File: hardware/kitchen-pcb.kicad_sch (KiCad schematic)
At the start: 40 parts, among them J1 GSD090012SEU, J2 Conn_02x02_Odd_Even, J3 Conn_01x06, J4 Conn_01x03, Q1 TEMT6000X01, U1 SHT30-DIS-B, U2 MX25L3233FM2I-08G

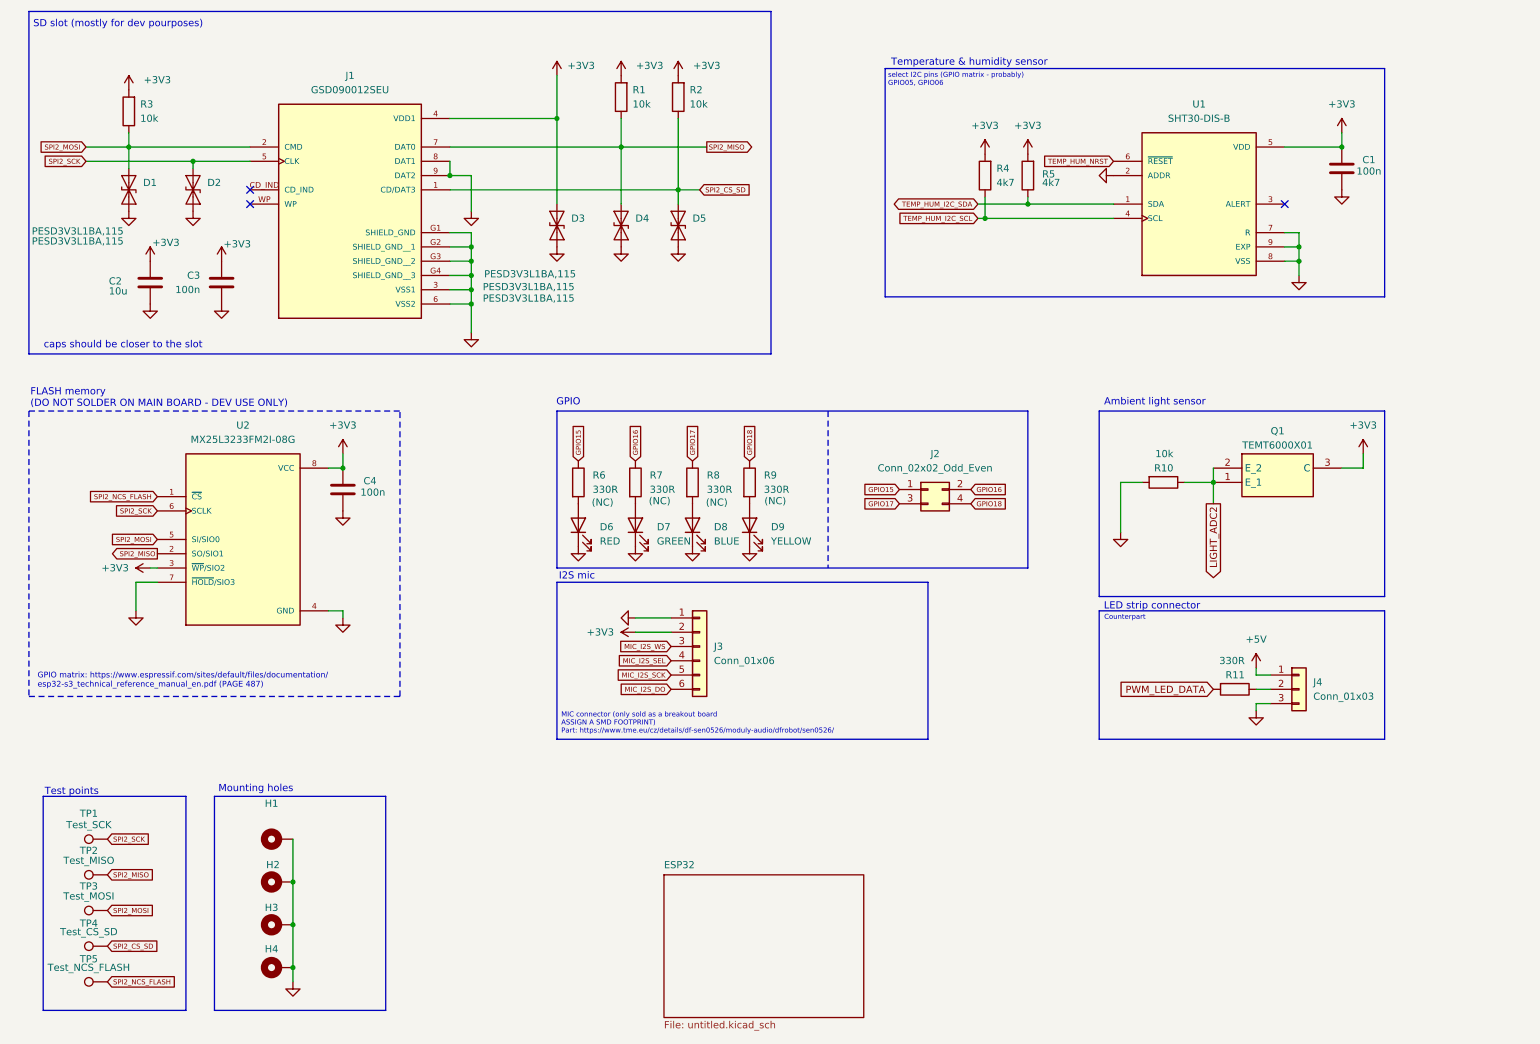
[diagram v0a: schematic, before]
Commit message: Added notes to schematics, SPI modifications
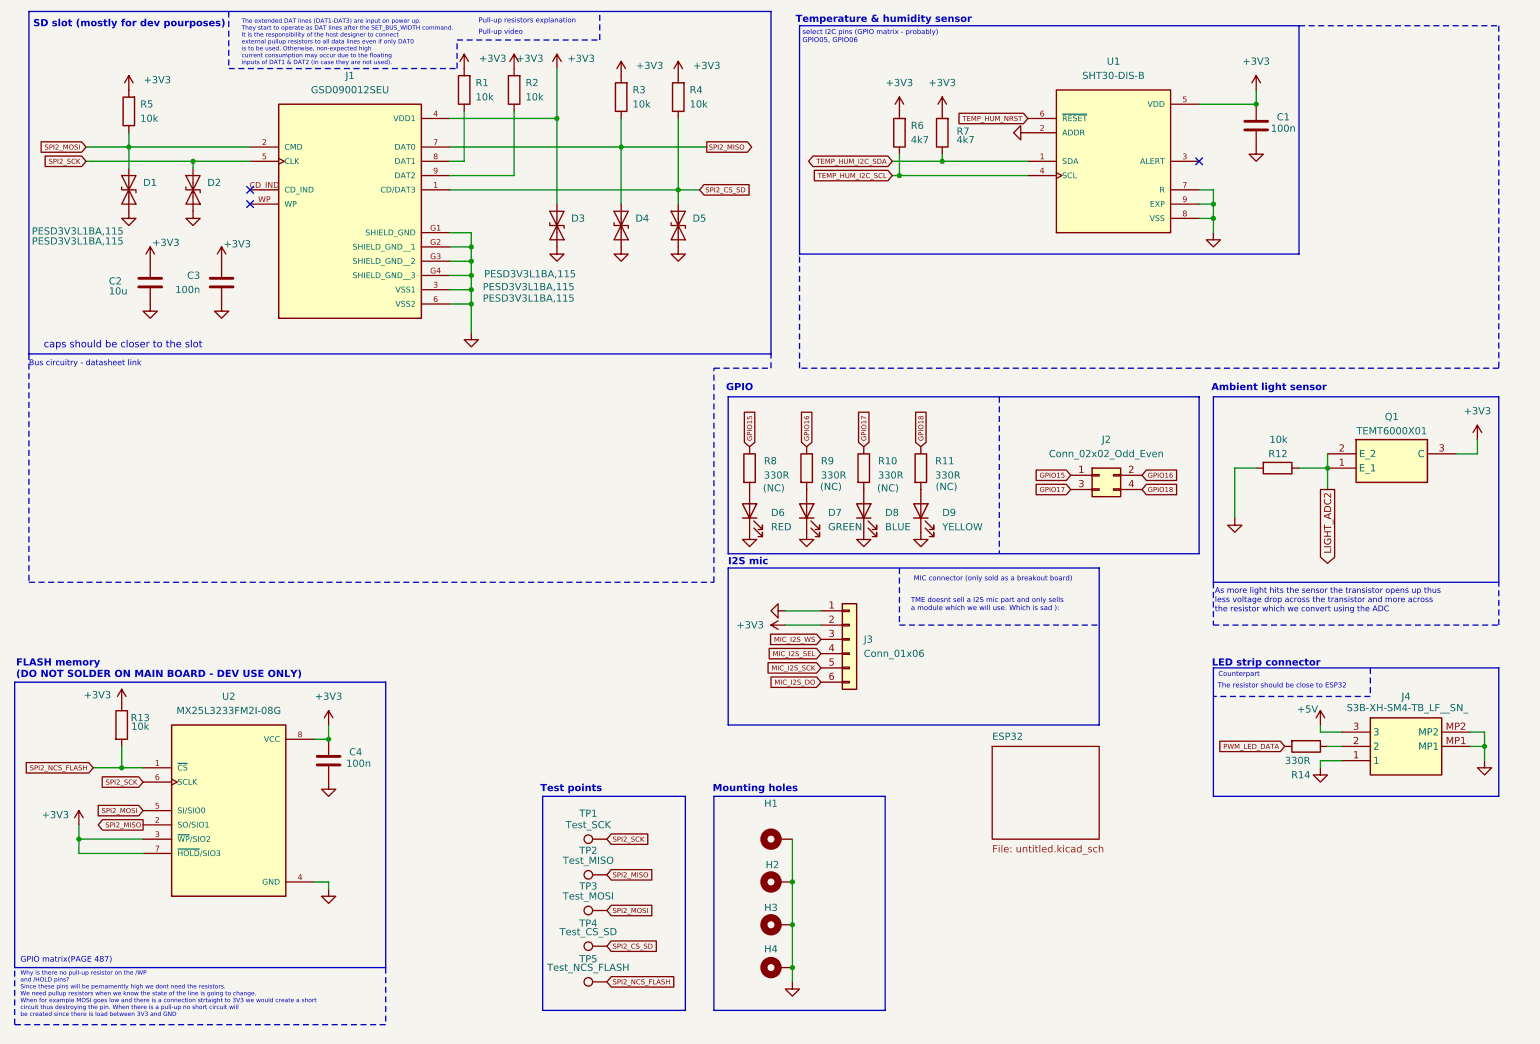
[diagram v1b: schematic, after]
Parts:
- removed J4: Conn_01x03, Connector_JST:JST_XH_S3B-XH-SM4-TB_1x03-1MP_P2.50mm_Horizontal, symbol Connector_Generic:Conn_01x03
- added J4: S3B-XH-SM4-TB_LF__SN_, ESP32-project-footprints:S3BXHSM4TBLFSN, symbol S3B-XH-SM4-TB_LF__SN_:S3B-XH-SM4-TB_LF__SN_
- added R1, R13, R2: 10k, Resistor_SMD:R_0805_2012Metric_Pad1.20x1.40mm_HandSolder, symbol Device:R
- renumbered R8 to R10, R9 to R11, R10 to R12, R11 to R14, R1 to R3, R2 to R4, R3 to R5, R4 to R6, R5 to R7, R6 to R8, R7 to R9
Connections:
- net +3V3: now also U2.7 (~{HOLD}/SIO3), R1.2, R13.1, R2.2
- net +5V: now also J4.3
- net GND: now also J4.1, J4.MP1, J4.MP2; no longer J1.8 (DAT1), J1.9 (DAT2), U2.7 (~{HOLD}/SIO3)
- net SPI2_NCS_FLASH: now also R13.2
- net at R14.1: now also J4.2
- new net: J1.9 (DAT2), R2.1
- new net: J1.8 (DAT1), R1.1
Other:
- note added: "As more light hits the sensor the transistor opens up thus less voltage drop across the transistor and more across the resistor which we convert using the ADC"
- note added: "Bus circuitry - datasheet link"
- note added: "GPIO matrix(PAGE 487)"
- note added: "MIC connector (only sold as a breakout board)"
- note added: "Pull-up resistors explanation"
- note added: "Pull-up video"
- note added: "TME doesnt sell a I2S mic part and only sells a module which we will use. Which is sad ):"
- note added: "The extended DAT lines (DAT1-DAT3) are input on power up. They start to operate as DAT lines after the SET_BUS_WIDTH command. It is the responsibility of the host designer to connect external pullup resistors to all data lines even if only DAT0 is to be used. Otherwise, non-expected high current consumption may occur due to the floating inputs of DAT1 & DAT2 (in case they are not used)."
- note added: "The resistor should be close to ESP32"
- note added: "Why is there no pull-up resistor on the /WP and /HOLD pins? Since these pins will be pernamently high we dont need the resistors. We need pullup resistors when we know the state of the line is going to change. When for example MOSI goes low and there is a connection strtaight to 3V3 we would create a short circuit thus destroying the pin. When there is a pull-up no short circuit will be created s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"
- note removed: "GPIO matrix: https://www.espressif.com/sites/default/files/documentation/ esp32-s3_technical_reference_manual_en.pdf (PAGE 487)"
- note removed: "MIC connector (only sold as a breakout board ASSIGN A SMD FOOTPRINT) Part: https://www.tme.eu/cz/details/df-sen0526/moduly-audio/dfrobot/sen0526/"
- moved on the sheet: C1, C4, D6, D7, D8, D9, H1, H2, H3, H4, J2, J3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

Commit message: Layout v0,4
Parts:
- TP1, TP2, TP3, TP4, TP5: footprint TestPoint:TestPoint_THTPad_D3.0mm_Drill1.5mm -> TestPoint:TestPoint_THTPad_D2.0mm_Drill1.0mm
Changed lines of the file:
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@@
 			)
 		)
-		(property "Footprint" "TestPoint:TestPoint_THTPad_D3.0mm_Drill1.5mm"
+		(property "Footprint" "TestPoint:TestPoint_THTPad_D2.0mm_Drill1.0mm"
 			(at 123.19 182.88 0)
 			(effects
@@
 			)
 		)
-		(property "Footprint" "TestPoint:TestPoint_THTPad_D3.0mm_Drill1.5mm"
+		(property "Footprint" "TestPoint:TestPoint_THTPad_D2.0mm_Drill1.0mm"
 			(at 123.19 157.48 0)
 			(effects
@@
 			)
 		)
-		(property "Footprint" "TestPoint:TestPoint_THTPad_D3.0mm_Drill1.5mm"
+		(property "Footprint" "TestPoint:TestPoint_THTPad_D2.0mm_Drill1.0mm"
 			(at 123.19 176.53 0)
 			(effects
@@
 			)
 		)
-		(property "Footprint" "TestPoint:TestPoint_THTPad_D3.0mm_Drill1.5mm"
+		(property "Footprint" "TestPoint:TestPoint_THTPad_D2.0mm_Drill1.0mm"
 			(at 123.19 170.18 0)
 			(effects
@@
 			)
 		)
-		(property "Footprint" "TestPoint:TestPoint_THTPad_D3.0mm_Drill1.5mm"
+		(property "Footprint" "TestPoint:TestPoint_THTPad_D2.0mm_Drill1.0mm"
 			(at 123.19 163.83 0)
 			(effects

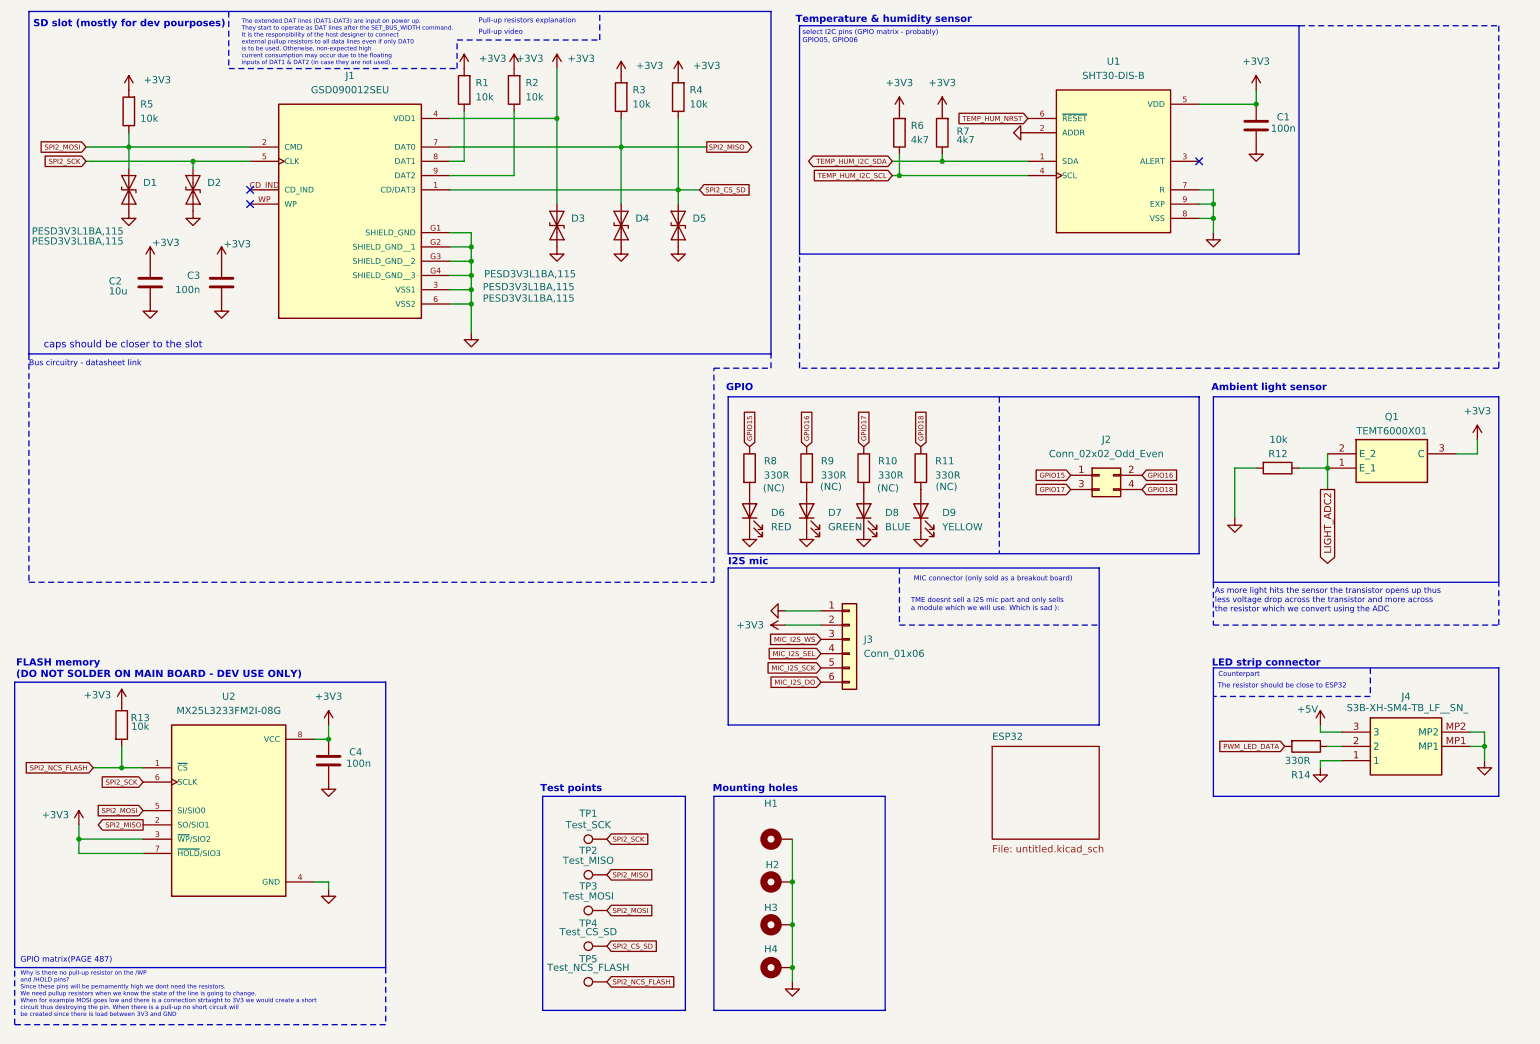
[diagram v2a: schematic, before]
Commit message: Changed to microSD, layout v0.6.1
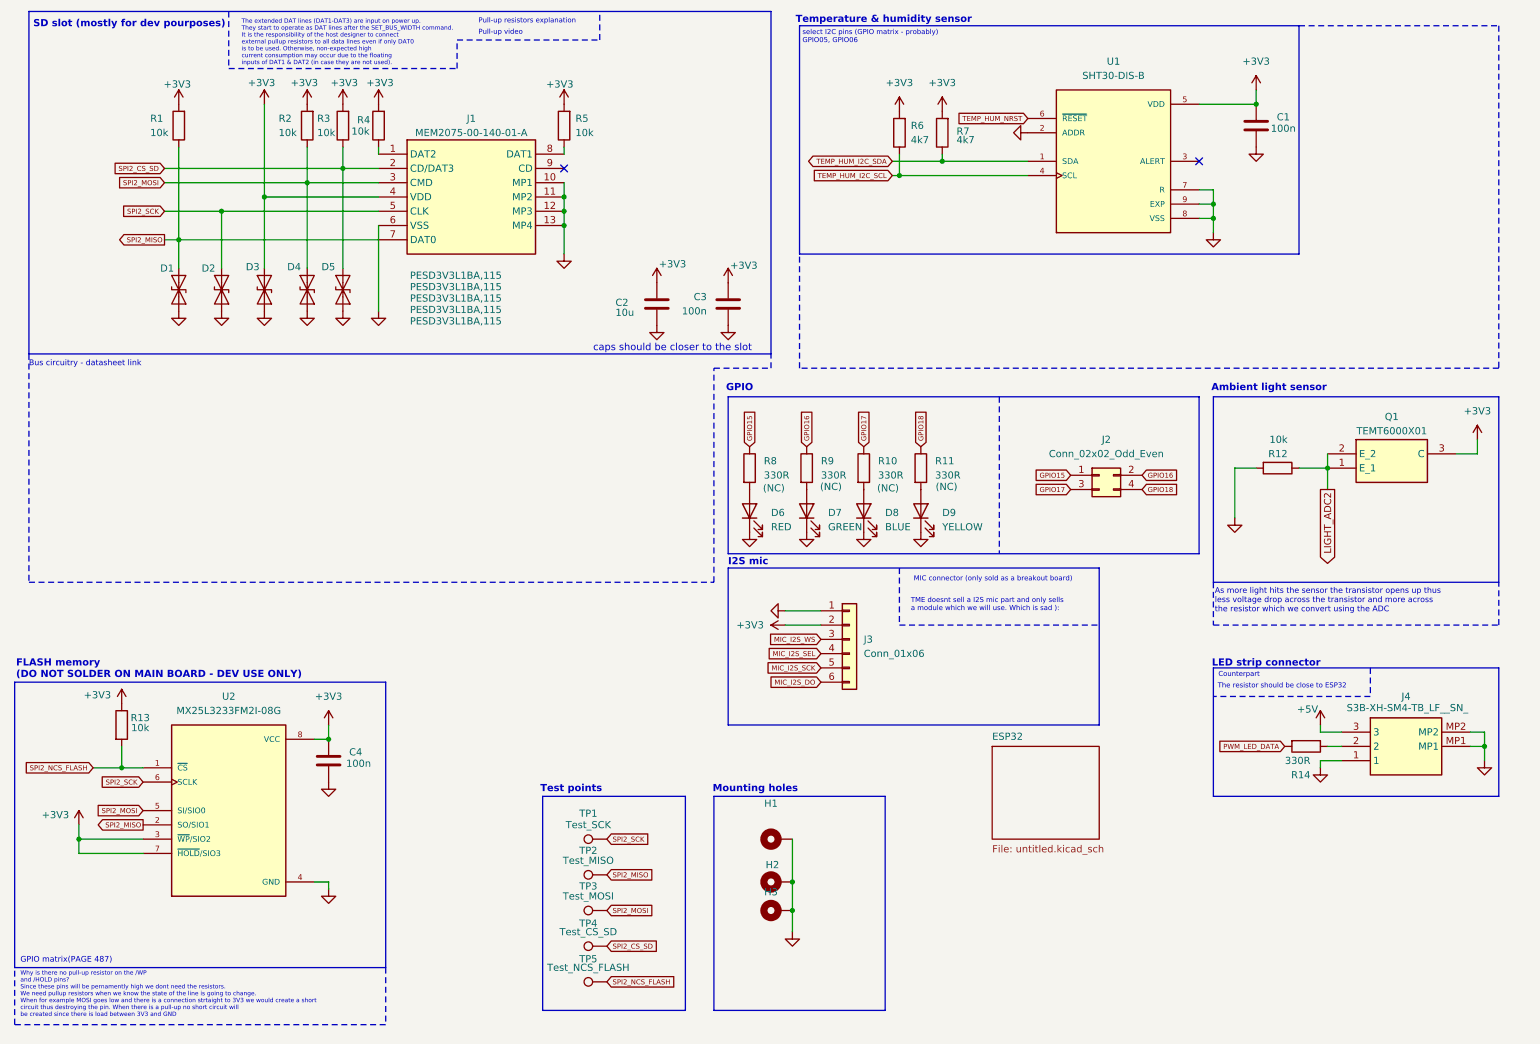
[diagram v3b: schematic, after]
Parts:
- removed H3: MountingHole_Pad, MountingHole:MountingHole_3.2mm_M3_DIN965_Pad_TopBottom, symbol Mechanical:MountingHole_Pad
- removed J1: GSD090012SEU, ESP32-project-footprints:AMPHENOL_GSD090012SEU, symbol GSD090012SEU:GSD090012SEU
- added J1: MEM2075-00-140-01-A, ESP32-project-footprints:MEM20750014001A, symbol MEM2075-00-140-01-A:MEM2075-00-140-01-A
- renumbered D4 to D1, D1 to D4, H4 to H3, R3 to R1, R5 to R2, R4 to R3, R1 to R4, R2 to R5
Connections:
- net +3V3: now also J1.4 (VDD)
- net GND: now also J1.10 (MP1), J1.11 (MP2), J1.12 (MP3), J1.13 (MP4), J1.6 (VSS)
- net SPI2_CS_SD: now also J1.2 (CD/DAT3)
- net SPI2_MISO: now also J1.7 (DAT0)
- net SPI2_MOSI: now also J1.3 (CMD)
- net SPI2_SCK: now also J1.5 (CLK)
- net at R5.1: now also J1.8 (DAT1)
- net at R4.1: now also J1.1 (DAT2)
- no-connect marks 3 -> 2
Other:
- moved on the sheet: C2, C3, D1, D2, D3, D4, D5, H3, R1, R2, R3, R4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

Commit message: Layout v0.6.2, SW1 footprint
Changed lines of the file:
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@@
 					(size 1.27 1.27)
 				)
+				(hide yes)
 			)
 		)
@@
 					(size 1.27 1.27)
 				)
+				(hide yes)
 			)
 		)
@@
 					(size 1.27 1.27)
 				)
+				(hide yes)
 			)
 		)
@@
 					(size 1.27 1.27)
 				)
+				(hide yes)
 			)
 		)
